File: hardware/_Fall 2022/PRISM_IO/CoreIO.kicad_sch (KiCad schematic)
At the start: 18 parts, among them J1 Conn_01x09_Female, Q1 Q_NJFET_DGS, U1 XT30UPB-M

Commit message: changed gitignore
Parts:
- removed D2: LED, symbol Device:LED
- removed H1, H2, H3, H4: Pad, symbol Mechanical:MountingHole_Pad
- removed J1: Conn_01x09_Female, Connector_JST:JST_PH_S9B-PH-K_1x09_P2.00mm_Horizontal, symbol Connector:Conn_01x09_Female
- removed Q1: Q_NJFET_DGS, symbol Device:Q_NJFET_DGS
- removed R6, R8, R?: R, symbol Device:R
- removed U1: XT30UPB-M, XT30UPB-M, symbol XT30:XT30UPB-M
- added BT? (x2): ~, symbol Device:Battery_Cell
- added C? (x2): 12uF, symbol Device:C
- added D? (x2): D_Zener, symbol Device:D_Zener
- added D?: SS14-Schottky, symbol Device:D_Schottky
- added D?: LED, symbol Device:LED
- added J?: Conn_01x07_Female, symbol Connector:Conn_01x07_Female
- added L?: 22uH, symbol pspice:INDUCTOR
- added PS?: ME2108A33P, CONV_ME2108A33P, symbol ME2108:ME2108A33P
- added Q? (x2): FQP27P06, Package_TO_SOT_THT:TO-220-3_Vertical, symbol Transistor_FET:FQP27P06
- added Q?: Q_NJFET_DGS, symbol Device:Q_NJFET_DGS
- added R? (x3): R, symbol Device:R
- added R? (x2): 100k, symbol Device:R
- added R?: 200k, symbol Device:R
- added SW?: SW_SPST, symbol Switch:SW_SPST
- added SW?: SW_DPST, symbol Switch:SW_DPST
- added U?: XT30UPB-M, XT30UPB-M, symbol XT30:XT30UPB-M
- R2: value R -> 100k
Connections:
- net ARM: now also J?.1 (Pin_1), R?.2
- net CONT 1: now also J?.3 (Pin_3)
- net CONT 2: now also J?.2 (Pin_2), R?.2
- net GND: now also BT?.2 (-), BT?.2 (-), C?.2, C?.2, J?.7 (Pin_7), PS?.1 (VSS), Q?.3 (S), R?.1, R?.1, R?.2, R?.2, R?.2
- net PYRO 1: now also J?.5 (Pin_5)
- net PYRO 2: now also J?.4 (Pin_4), Q?.2 (G), R?.1
- net V_IGNITOR: now also SW?.1 (A), U?.P$2 (-)
- net VCC renamed Switch1
- net Switch1: now also Q?.2 (D), SW?.3
- new net: D?.2 (A), Q?.1 (G), R?.1 (x2)
- new net: D?.2 (A), L?.2, PS?.3 (LX)
- new net: Q?.1 (D), R?.1, U?.P$1 (+)
- new net: D?.1 (K), R?.2
- new net 5V: C?.1, C?.1, D?.1 (K), J?.6 (Pin_6), PS?.2 (VOUT), SW?.2 (B)
- new net BAT1: D?.1 (K), D?.1 (K), L?.1, Q?.3 (S), Q?.3 (S)
- new net Bat_V1: BT?.1 (+), SW?.4
- new net Bat_V2: BT?.1 (+), SW?.2
- new net Switch2: D?.2 (A), Q?.2 (D), SW?.1
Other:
- note added: "Battery 1"
- note added: "Battery 2"
- note added: "Boost Converter 3v3 to Teensy 5v"
- note added: "EMATCH1"
- note added: "EMATCH2"
- note added: "Terminals to Electromechanical Arming Switch"
- moved on the sheet: D1, Q?, R1, R2, R?, U?

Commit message: Power board changes
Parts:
- R1, R?: value R -> 10k
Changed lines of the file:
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@@
+    (stroke (width 0) (type default) (color 0 0 0 0))
+  )
+  (polyline (pts (xy 24.13 97.79) (xy 170.18 97.79))
     (stroke (width 0) (type default) (color 0 0 0 0))
   )
@@
     (stroke (width 0) (type default) (color 0 0 0 0))
   )
+  (polyline (pts (xy 170.18 190.5) (xy 16.51 190.5))
+    (stroke (width 0) (type default) (color 0 0 0 0))
+  )
   (wire (pts (xy 204.47 58.42) (xy 204.47 83.82))
     (stroke (width 0) (type default) (color 0 0 0 0))
@@
     (stroke (width 0) (type default) (color 0 0 0 0))
   )
+  (polyline (pts (xy 16.51 190.5) (xy 16.51 97.79))
+    (stroke (width 0) (type default) (color 0 0 0 0))
+  )
   (wire (pts (xy 35.56 153.67) (xy 38.1 153.67))
     (stroke (width 0) (type default) (color 0 0 0 0))
@@
     (stroke (width 0) (type default) (color 0 0 0 0))
   )
+  (polyline (pts (xy 16.51 97.79) (xy 76.2 97.79))
+    (stroke (width 0) (type default) (color 0 0 0 0))
+  )
   (wire (pts (xy 133.35 69.85) (xy 139.7 69.85))
     (stroke (width 0) (type default) (color 0 0 0 0))
@@
   )
   (wire (pts (xy 243.84 25.4) (xy 243.84 36.83))
+    (stroke (width 0) (type default) (color 0 0 0 0))
+  )
+  (polyline (pts (xy 170.18 97.79) (xy 170.18 190.5))
     (stroke (width 0) (type default) (color 0 0 0 0))
   )
@@
       (effects (font (size 1.27 1.27)) (justify right))
     )
-    (property "Value" "R" (id 1) (at 97.79 68.5799 0)
+    (property "Value" "10k" (id 1) (at 97.79 68.5799 0)
       (effects (font (size 1.27 1.27)) (justify right))
     )
@@
       (effects (font (size 1.27 1.27)) (justify right))
     )
-    (property "Value" "R" (id 1) (at 102.87 68.5799 0)
+    (property "Value" "10k" (id 1) (at 102.87 68.5799 0)
       (effects (font (size 1.27 1.27)) (justify right))
     )
@@
     )
     (path "/2431e708-6d96-4879-b804-744396cc6ea4"
-      (reference "R1") (unit 1) (value "R") (footprint "")
+      (reference "R1") (unit 1) (value "10k") (footprint "")
     )
     (path "/90e70778-87cc-48a2-850f-e02db16d561d"
@@
     )
     (path "/cc6575c1-19aa-4a63-82fe-a2ddcc2f6143"
-      (reference "R?") (unit 1) (value "R") (footprint "")
+      (reference "R?") (unit 1) (value "10k") (footprint "")
     )
     (path "/da01c7bf-6619-4764-9ff9-27e28e08c3c6"

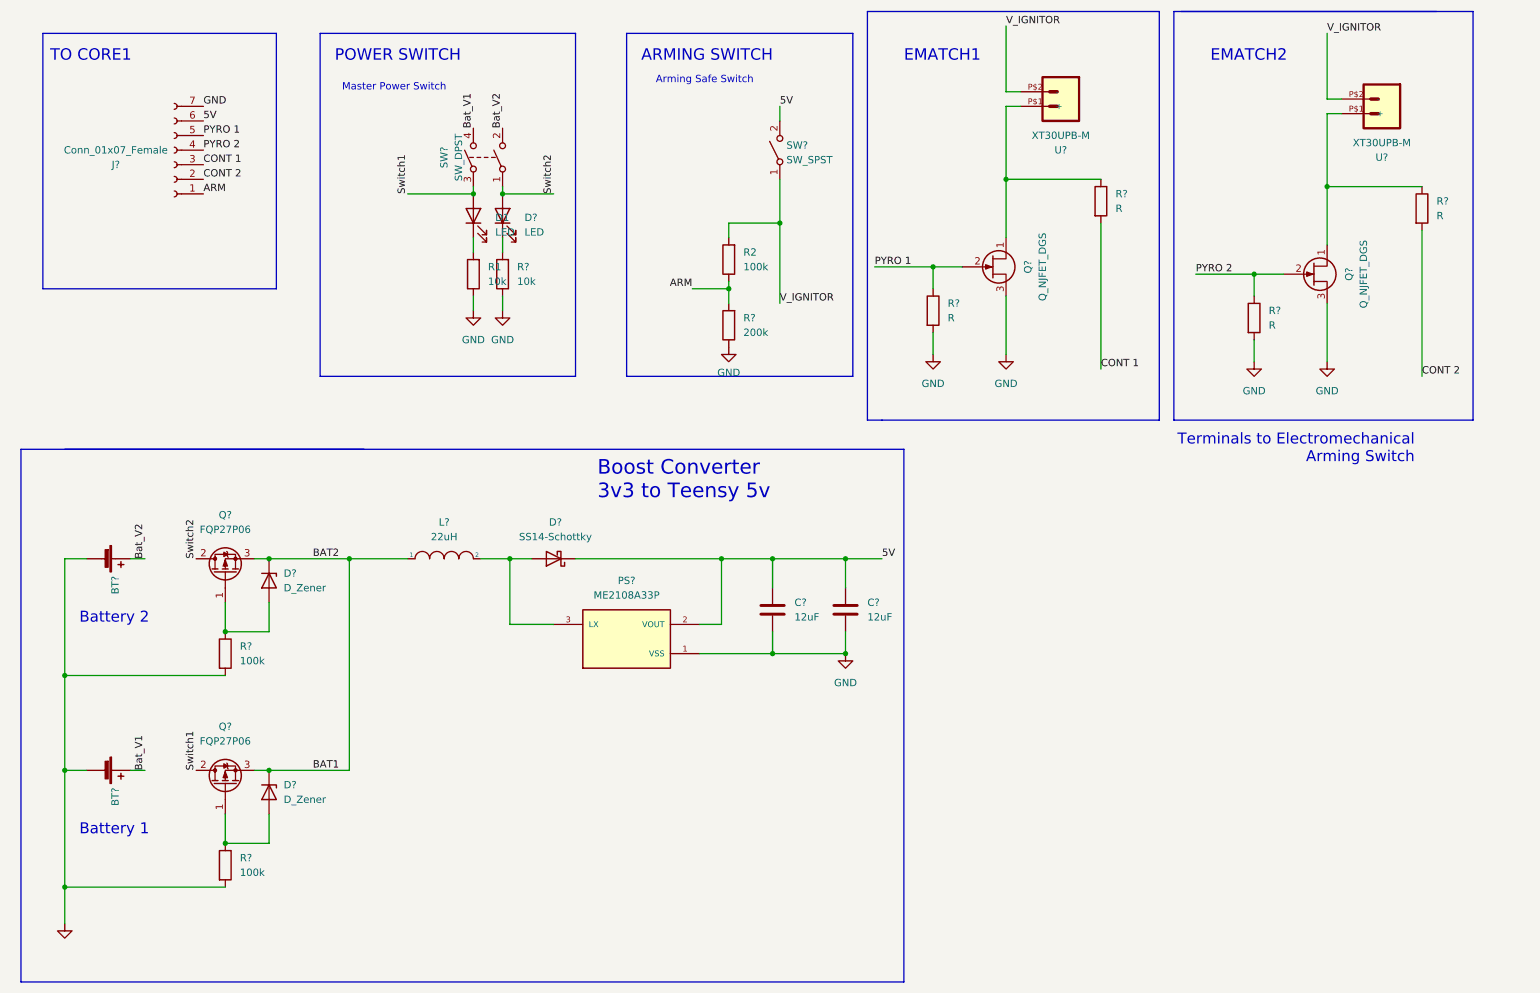
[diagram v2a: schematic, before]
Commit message: Removed files
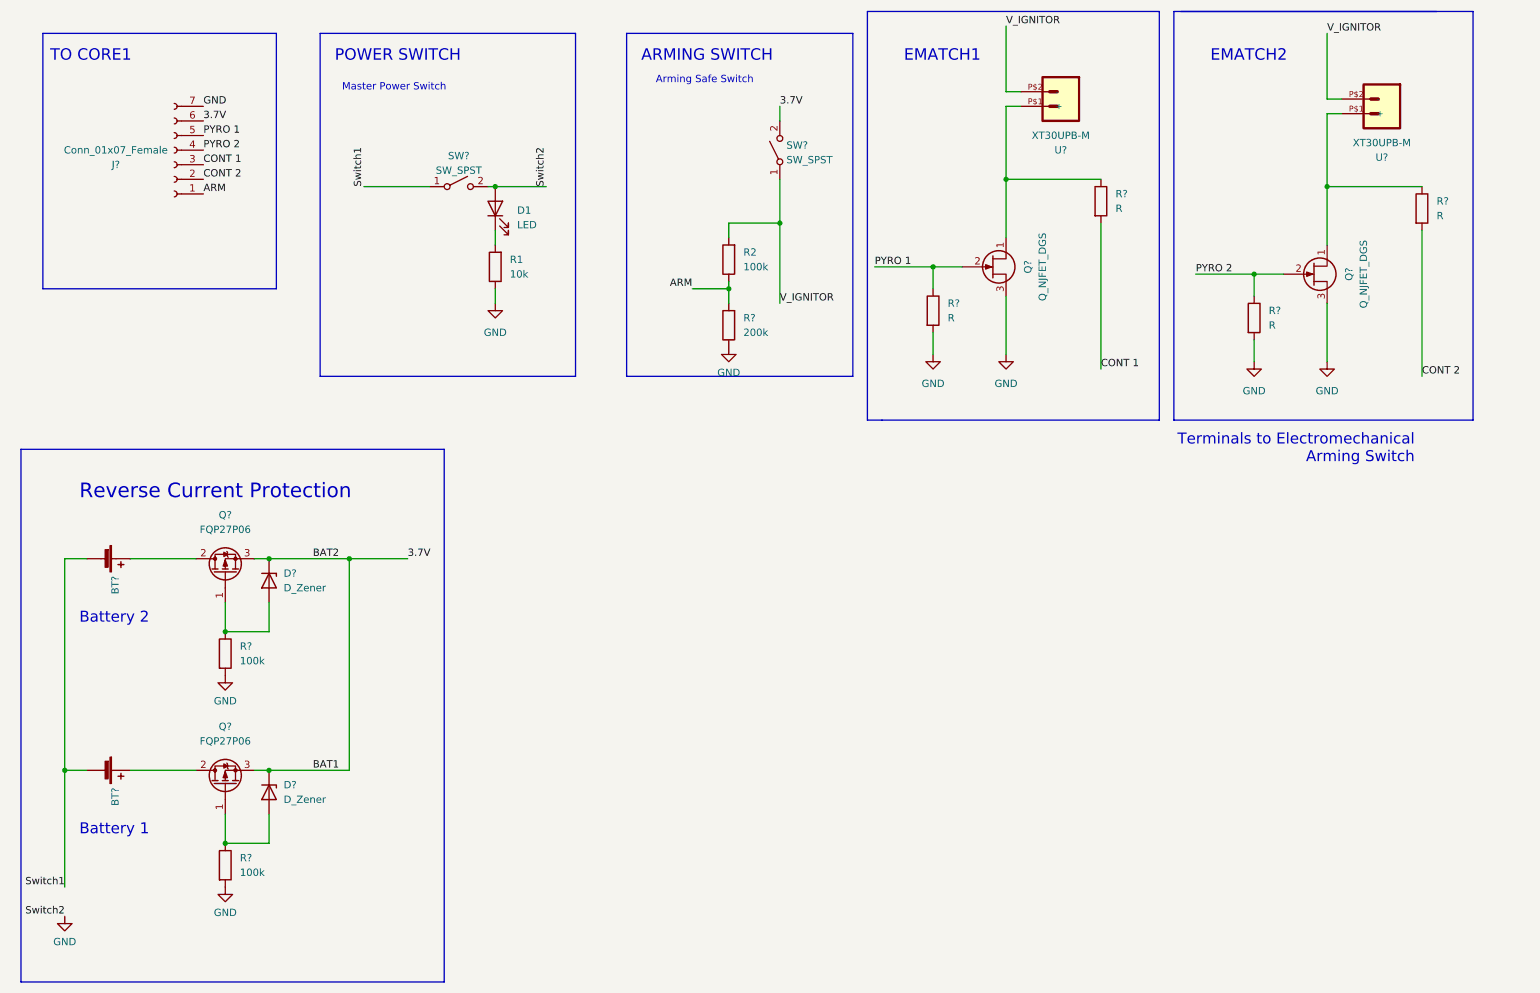
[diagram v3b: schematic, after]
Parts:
- removed C? (x2): 12uF, symbol Device:C
- removed D?: SS14-Schottky, symbol Device:D_Schottky
- removed D?: LED, symbol Device:LED
- removed L?: 22uH, symbol pspice:INDUCTOR
- removed PS?: ME2108A33P, CONV_ME2108A33P, symbol ME2108:ME2108A33P
- removed R?: 10k, symbol Device:R
- removed SW?: SW_DPST, symbol Switch:SW_DPST
- added SW?: SW_SPST, symbol Switch:SW_SPST
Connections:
- net BAT1 is gone; now on net 3.7V: D?.1 (K), D?.1 (K), Q?.3 (S), Q?.3 (S)
- net Switch2 is gone; now on an unnamed net: Q?.2 (D)
- net GND: now also D1.2 (A), SW?.2 (B); no longer BT?.2 (-), BT?.2 (-)
- net Switch1: now also BT?.2 (-), BT?.2 (-), SW?.1 (A); no longer D1.2 (A), Q?.2 (D)
- net 5V renamed 3.7V
- net Bat_V1: no longer names the net of BT?.1 (+)
- net Bat_V1: now also Q?.2 (D)
- net Bat_V2: no longer names the net of BT?.1 (+)
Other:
- note added: "Reverse Current Protection"
- note removed: "Boost Converter 3v3 to Teensy 5v"
- moved on the sheet: D1, R1

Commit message: add footprint for IO connector
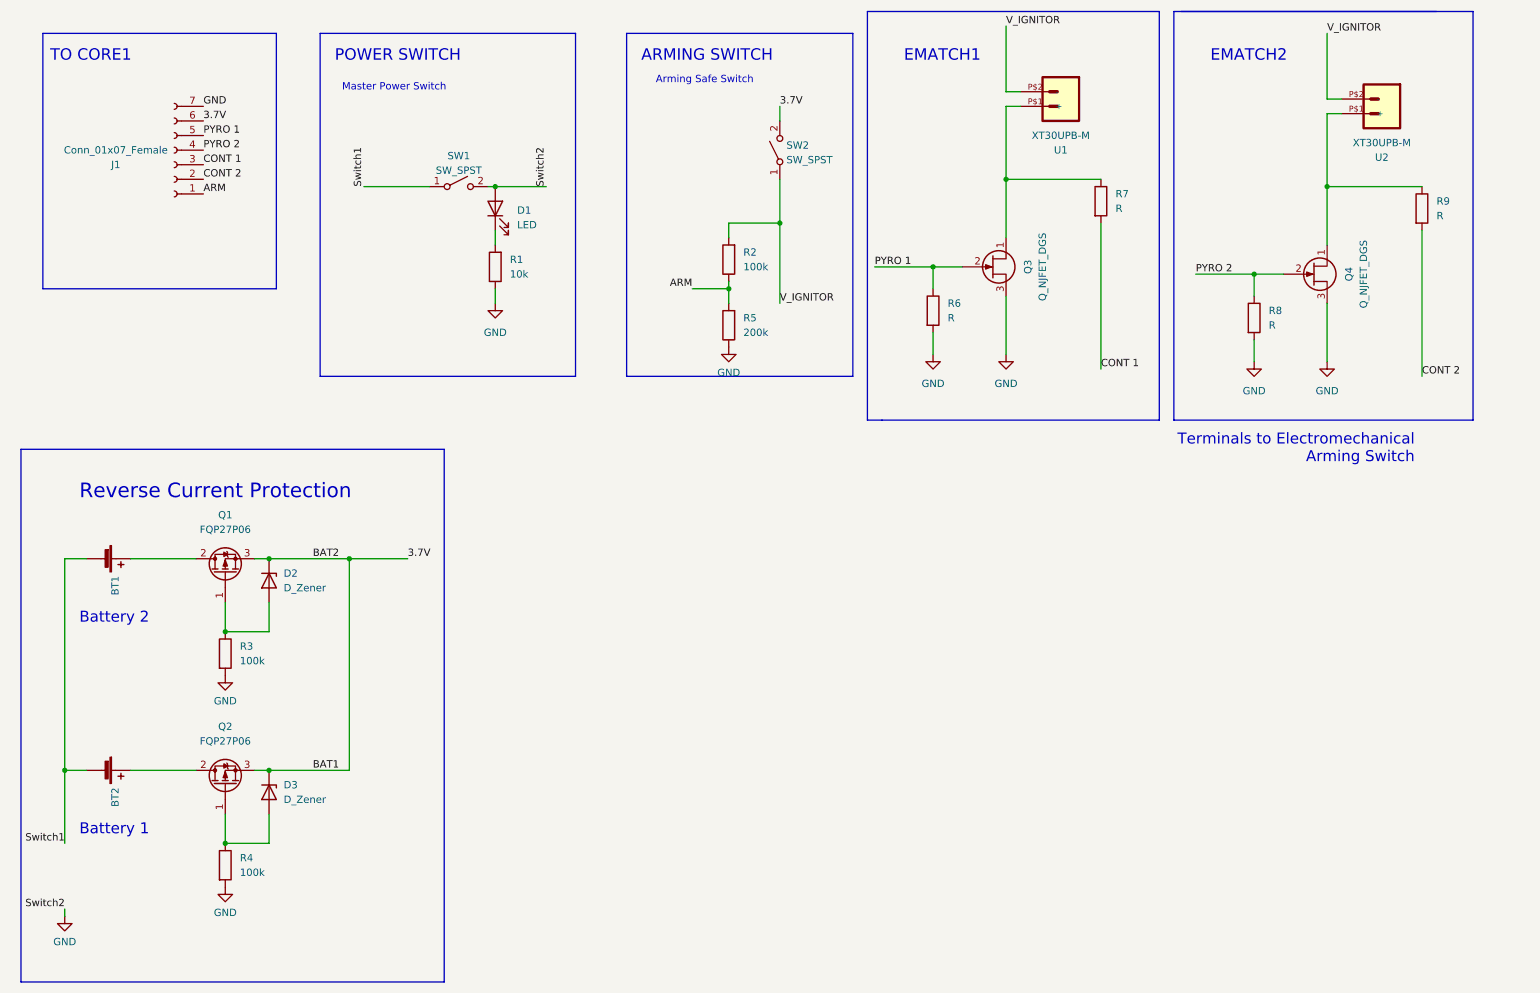
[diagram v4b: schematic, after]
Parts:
- J1: renamed from J?; footprint (none) -> JST:JST_PH_S7B-PH-K_07x2.00mm_Angled
- U1: renamed from U?; footprint XT30UPB-M -> Connector_AMASS:AMASS_XT30U-F_1x02_P5.0mm_Vertical
- gave numbers to parts that had none: 18
